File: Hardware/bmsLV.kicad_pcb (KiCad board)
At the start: 2 copper layers, 121.2 x 60.6 mm, 160 parts, among them J1 Conn_01x06_Male, J10 Conn_01x01_Female, J11 Conn_01x01_Female, J12 Conn_01x01_Female, J13 Conn_01x04_Male, J14 Conn_01x02_Male, J15 Conn_01x02_Male, J16 Conn_01x02_Male, J17 Conn_01x02_Male, J2 USB_B_Mini, J3 Conn_01x02_Female, J4 Conn_01x02_Male, J5 CAN conn, J6 Conn_01x01_Female, J7 Conn_01x01_Female, J8 Conn_01x01_Female, J9 Conn_01x01_Female, K1 RM85V7, Q1 BSS138, Q2 Q_NMOS_GSD, Q3 Q_NMOS_GSD, Q4 Q_NMOS_GSD, Q5 Q_NMOS_GSD, Q6 Q_NMOS_GSD, Q7 Q_NMOS_GSD, Q8 BSS138, Q9 Q_NPN_BCE, SW1 SW_Push, U2 LM1117-3.3, U3 LM2596S-5, U4 MCP2562-H-SN, U5 STM32L4P5RET6, Y1 Crystal

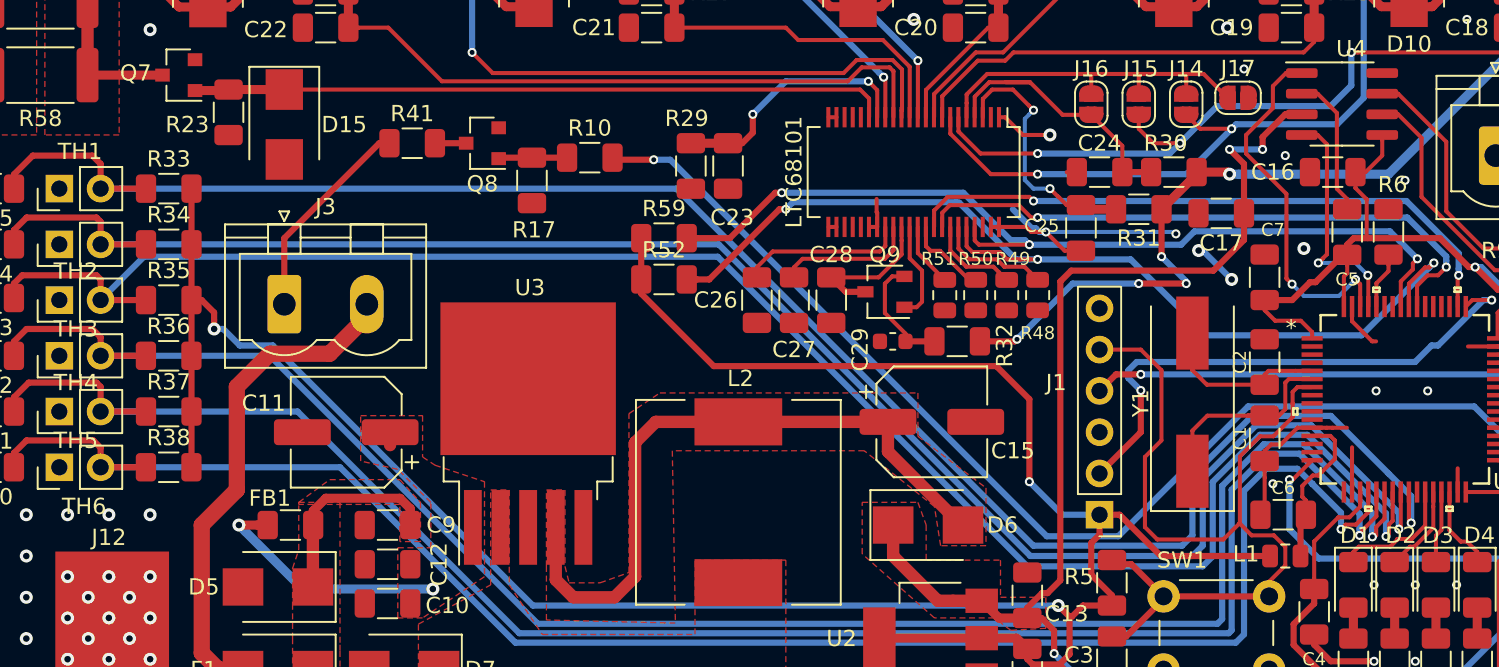
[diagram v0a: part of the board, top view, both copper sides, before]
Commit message: CS and CLK pull up added
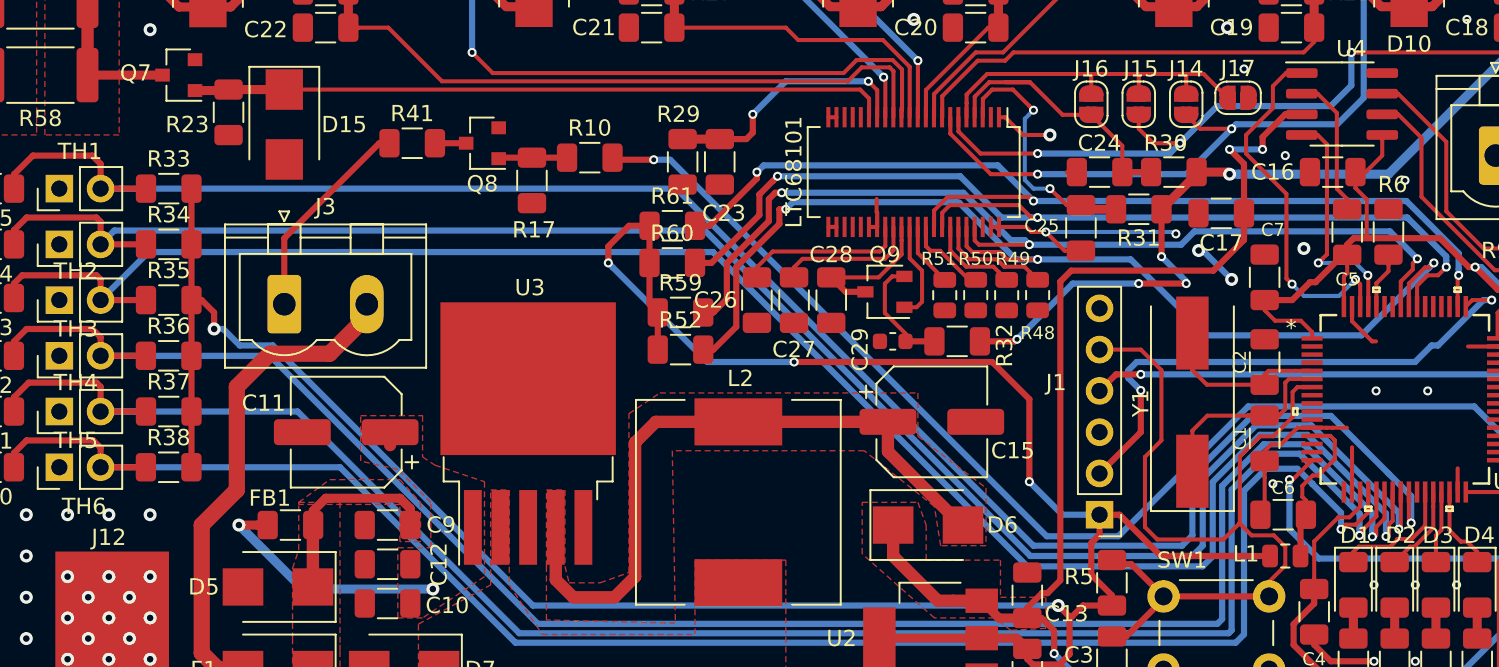
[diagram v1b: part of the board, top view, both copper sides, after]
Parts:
- added R60: 2.2k, Resistor_SMD:R_1206_3216Metric, F.Cu at (62.6, 89.9)
- added R61: 2.2k, Resistor_SMD:R_1206_3216Metric, F.Cu at (62.6, 87.6)
- moved R59 4.68 mm to (63.1, 93.0)
- moved R52 4.44 mm to (63.1, 95.2)
- moved C23 0.57 mm to (65.5, 83.7)
- moved R29 0.57 mm to (63.2, 83.7)
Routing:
- net SCK: track 37.6 -> 62.7 mm, vias 2 -> 3
- net CS: track 38.4 -> 61.9 mm, vias 2 -> 3
- net SW_VDD: track 274.8 -> 286.1 mm, vias 5 -> 7
- net MISO: track 62.6 -> 66.0 mm
- net MOSI: track 56.1 -> 59.1 mm
- net SW_GND: track 83.6 -> 81.0 mm
- net Term_5: track 110.7 -> 111.4 mm

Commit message: Checked By SS
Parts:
- moved R48 0.25 mm to (84.8, 91.9)
- moved R49 0.25 mm to (82.9, 91.9)
- moved R50 0.25 mm to (81.0, 91.9)
- moved R51 0.25 mm to (79.1, 91.9)
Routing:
- net SW_GND: track 81.0 -> 86.1 mm
- net Term_6: track 112.1 -> 109.4 mm
- net Term_4: track 111.3 -> 108.6 mm
- net Term_5: track 111.4 -> 109.0 mm
- net +24V: track 76.4 -> 74.3 mm, vias 118 -> 114
- net +5V: track 99.4 -> 97.6 mm
- net Term_1: track 106.6 -> 105.3 mm
- net Term_2: track 109.8 -> 108.6 mm
- net MISO: track 66.0 -> 64.8 mm
- net Term_3: track 111.5 -> 110.5 mm
- net TX_Can: track 22.6 -> 22.0 mm

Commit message: PUTM Logos added
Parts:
- added G***: LOGO, Logos:SignatureBox50mm, B.Cu at (66.0, 75.7)
- added G***: LOGO, Logos:PUTM_LOGO_35mm, B.Cu at (66.3, 101.9)
- added G***: LOGO, Logos:PUTM_LOGO_13mm, F.Cu at (54.4, 80.0)
- moved Q8 2.59 mm to (50.4, 85.1)
- moved R17 2.59 mm to (53.5, 87.4)
- moved R41 2.59 mm to (46.1, 85.1)
- moved R10 2.59 mm to (57.0, 86.0)
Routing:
- net Term_3: track 110.5 -> 106.4 mm
- net Term_2: track 108.6 -> 104.8 mm
- net LED_D: track 72.7 -> 74.1 mm
- net Term_1: track 105.3 -> 104.0 mm
- net LED_D_OUT: track 13.0 -> 12.0 mm
- net SW_GND: vias 59 -> 60

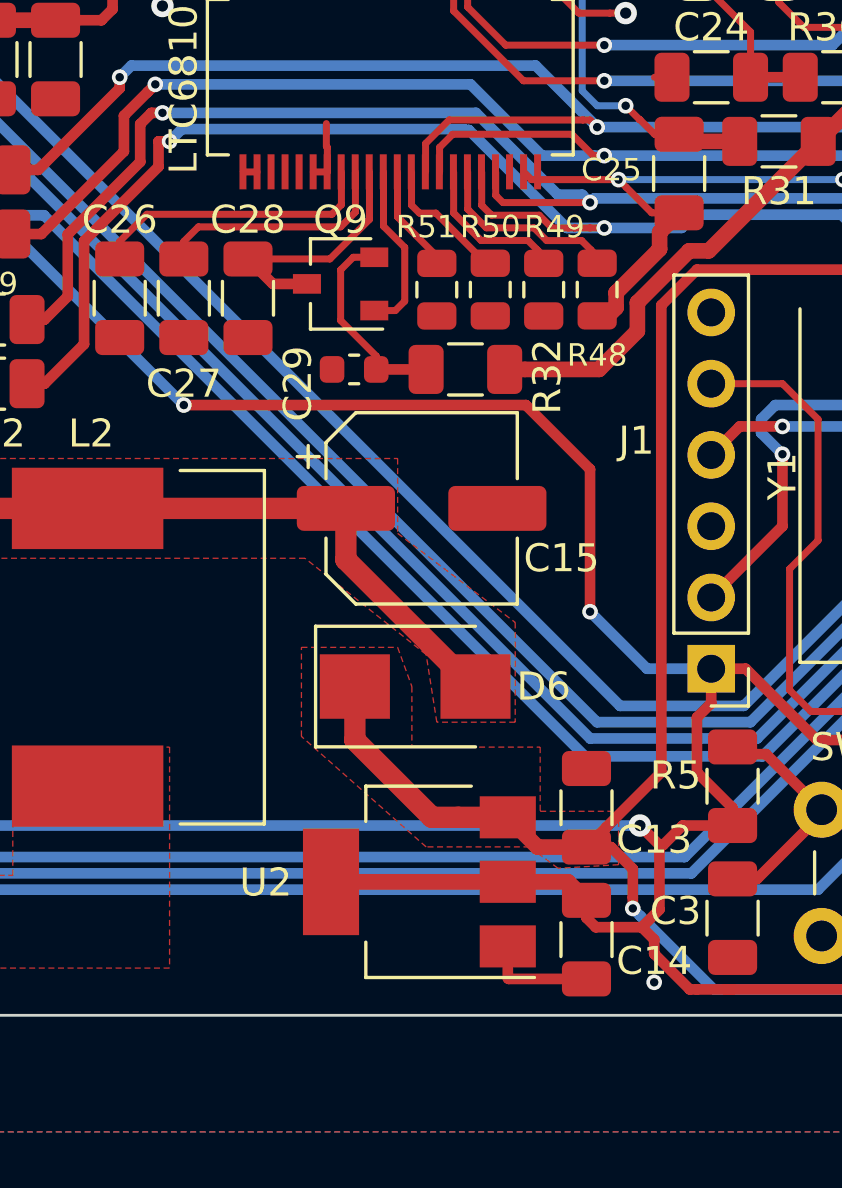
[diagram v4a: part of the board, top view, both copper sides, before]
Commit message: gitignore modified
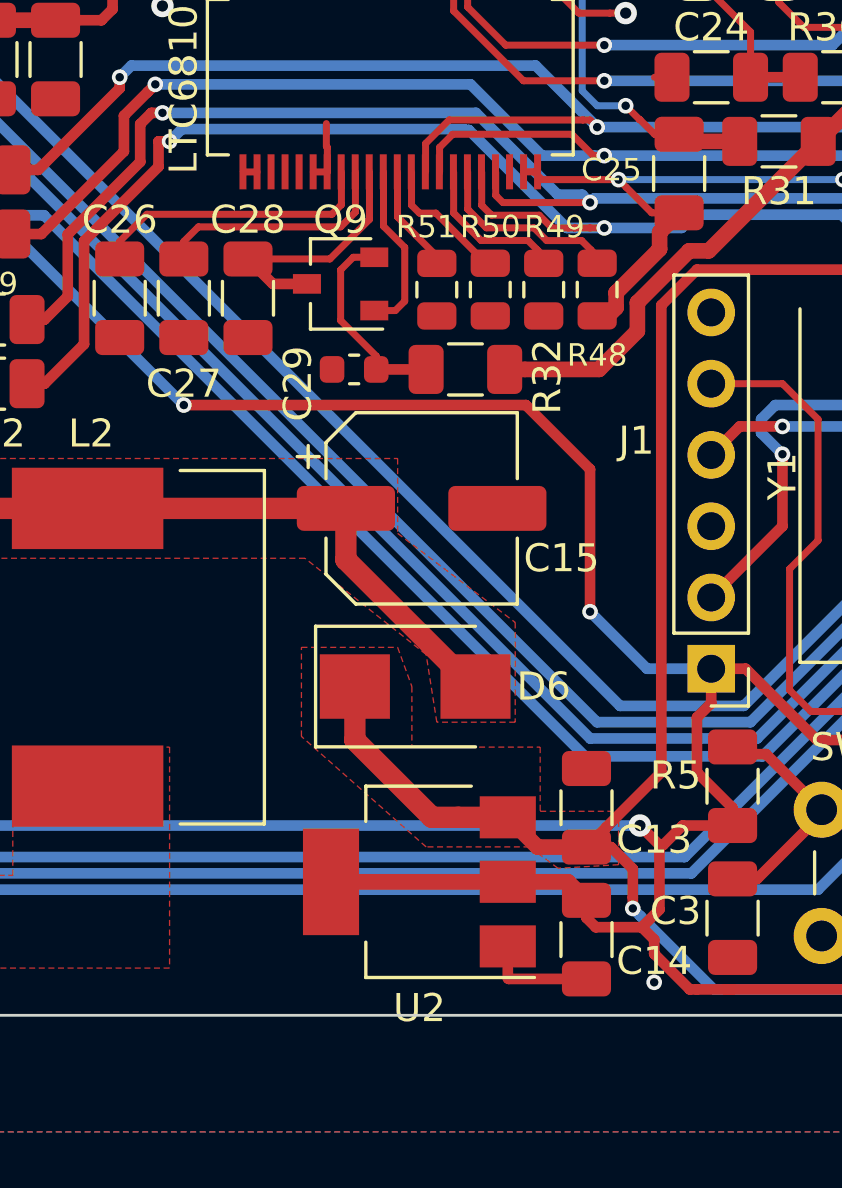
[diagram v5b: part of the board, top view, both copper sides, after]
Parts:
- U2: footprint Package_TO_SOT_SMD:SOT-223 -> Package_TO_SOT_SMD:SOT-223-3_TabPin2
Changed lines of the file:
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@@
     (thickness 1.6)
     (drawings 4)
-    (tracks 1311)
+    (tracks 1312)
     (zones 0)
     (modules 165)
@@
     (pcbplotparams
       (layerselection 0x010fc_ffffffff)
-      (usegerberextensions false)
+      (usegerberextensions true)
       (usegerberattributes false)
       (usegerberadvancedattributes false)
@@
       (psa4output false)
       (plotreference true)
-      (plotvalue true)
+      (plotvalue false)
       (plotinvisibletext false)
       (padsonsilk false)
-      (subtractmaskfromsilk false)
+      (subtractmaskfromsilk true)
       (outputformat 1)
       (mirror false)
-      (drillshape 1)
+      (drillshape 0)
       (scaleselection 1)
-      (outputdirectory ""))
+      (outputdirectory "PUTM_EV_BMS_LV_GERBERS/"))
   )
   (net 0 "")
@@
     (add_net V_Out)
   )
+  (module Package_TO_SOT_SMD:SOT-223-3_TabPin2 (layer F.Cu)
+    (at 78.5 113.005 180)
+    (descr "module CMS SOT223 4 pins")
+    (tags "CMS SOT")
+    (attr smd)
+    (fp_text reference U2 (at 0 -4.5) (layer F.SilkS)
+      (effects (font (size 1 1) (thickness 0.15)))
+    )
+    (fp_text value LM1117-3.3 (at 0 4.5) (layer F.Fab)
+      (effects (font (size 1 1) (thickness 0.15)))
+    )
+    (fp_line (start 1.85 -3.35) (end 1.85 3.35) (layer F.Fab) (width 0.1))
+    (fp_line (start -1.85 3.35) (end 1.85 3.35) (layer F.Fab) (width 0.1))
+    (fp_line (start -4.1 -3.41) (end 1.91 -3.41) (layer F.SilkS) (width 0.12))
+    (fp_line (start -0.85 -3.35) (end 1.85 -3.35) (layer F.Fab) (width 0.1))
+    (fp_line (start -1.85 3.41) (end 1.91 3.41) (layer F.SilkS) (width 0.12))
+    (fp_line (start -1.85 -2.35) (end -1.85 3.35) (layer F.Fab) (width 0.1))
+    (fp_line (start -1.85 -2.35) (end -0.85 -3.35) (layer F.Fab) (width 0.1))
+    (fp_line (start -4.4 -3.6) (end -4.4 3.6) (layer F.CrtYd) (width 0.05))
+    (fp_line (start -4.4 3.6) (end 4.4 3.6) (layer F.CrtYd) (width 0.05))
+    (fp_line (start 4.4 3.6) (end 4.4 -3.6) (layer F.CrtYd) (width 0.05))
+    (fp_line (start 4.4 -3.6) (end -4.4 -3.6) (layer F.CrtYd) (width 0.05))
+    (fp_line (start 1.91 -3.41) (end 1.91 -2.15) (layer F.SilkS) (width 0.12))
+    (fp_line (start 1.91 3.41) (end 1.91 2.15) (layer F.SilkS) (width 0.12))
+    (fp_text user %R (at 0 0 90) (layer F.Fab)
+      (effects (font (size 0.8 0.8) (thickness 0.12)))
+    )
+    (pad 1 smd rect (at -3.15 -2.3 180) (size 2 1.5) (layers F.Cu F.Paste F.Mask)
+      (net 1 SW_GND))
+    (pad 3 smd rect (at -3.15 2.3 180) (size 2 1.5) (layers F.Cu F.Paste F.Mask)
+      (net 6 +5V))
+    (pad 2 smd rect (at -3.15 0 180) (size 2 1.5) (layers F.Cu F.Paste F.Mask)
+      (net 3 SW_VDD))
+    (pad 2 smd rect (at 3.15 0 180) (size 2 3.8) (layers F.Cu F.Paste F.Mask)
+      (net 3 SW_VDD))
+    (model ${KISYS3DMOD}/Package_TO_SOT_SMD.3dshapes/SOT-223.wrl
+      (at (xyz 0 0 0))
+      (scale (xyz 1 1 1))
+      (rotate (xyz 0 0 0))
+    )
+  )
   (module Logos:SignatureBox50mm (layer B.Cu)
     (at 66.04 75.692)
@@
     )
   )
-  (module Package_TO_SOT_SMD:SOT-223 (layer F.Cu)
-    (at 78.5 113.005 180)
-    (descr "module CMS SOT223 4 pins")
-    (tags "CMS SOT")
-    (attr smd)
-    (fp_text reference U2 (at 5.475 -0.025 180) (layer F.SilkS)
-      (effects (font (size 1 1) (thickness 0.15)))
-    )
-    (fp_text value LM1117-3.3 (at 0 4.5) (layer F.Fab)
-      (effects (font (size 1 1) (thickness 0.15)))
-    )
-    (fp_text user %R (at 0 0 90) (layer F.Fab)
-      (effects (font (size 0.8 0.8) (thickness 0.12)))
-    )
-    (fp_line (start -1.85 -2.3) (end -0.8 -3.35) (layer F.Fab) (width 0.1))
-    (fp_line (start 1.91 3.41) (end 1.91 2.15) (layer F.SilkS) (width 0.12))
-    (fp_line (start 1.91 -3.41) (end 1.91 -2.15) (layer F.SilkS) (width 0.12))
-    (fp_line (start 4.4 -3.6) (end -4.4 -3.6) (layer F.CrtYd) (width 0.05))
-    (fp_line (start 4.4 3.6) (end 4.4 -3.6) (layer F.CrtYd) (width 0.05))
-    (fp_line (start -4.4 3.6) (end 4.4 3.6) (layer F.CrtYd) (width 0.05))
-    (fp_line (start -4.4 -3.6) (end -4.4 3.6) (layer F.CrtYd) (width 0.05))
-    (fp_line (start -1.85 -2.3) (end -1.85 3.35) (layer F.Fab) (width 0.1))
-    (fp_line (start -1.85 3.41) (end 1.91 3.41) (layer F.SilkS) (width 0.12))
-    (fp_line (start -0.8 -3.35) (end 1.85 -3.35) (layer F.Fab) (width 0.1))
-    (fp_line (start -4.1 -3.41) (end 1.91 -3.41) (layer F.SilkS) (width 0.12))
-    (fp_line (start -1.85 3.35) (end 1.85 3.35) (layer F.Fab) (width 0.1))
-    (fp_line (start 1.85 -3.35) (end 1.85 3.35) (layer F.Fab) (width 0.1))
-    (pad 4 smd rect (at 3.15 0 180) (size 2 3.8) (layers F.Cu F.Paste F.Mask))
-    (pad 2 smd rect (at -3.15 0 180) (size 2 1.5) (layers F.Cu F.Paste F.Mask)
-      (net 3 SW_VDD))
-    (pad 3 smd rect (at -3.15 2.3 180) (size 2 1.5) (layers F.Cu F.Paste F.Mask)
-      (net 6 +5V))
-    (pad 1 smd rect (at -3.15 -2.3 180) (size 2 1.5) (layers F.Cu F.Paste F.Mask)
-      (net 1 SW_GND))
-    (model ${KISYS3DMOD}/Package_TO_SOT_SMD.3dshapes/SOT-223.wrl
-      (at (xyz 0 0 0))
-      (scale (xyz 1 1 1))
-      (rotate (xyz 0 0 0))
-    )
-  )
   (module Button_Switch_THT:SW_PUSH_6mm (layer F.Cu)
     (at 92.837 110.435)
@@
   (segment (start 85.876999 88.255489) (end 85.598 87.97649) (width 0.25) (layer F.Cu) (net 1))
   (segment (start 87.757 89.16) (end 86.78151 89.16) (width 0.25) (layer F.Cu) (net 1))
-  (segment (start 85.203435 87.97649) (end 85.598 87.97649) (width 0.25) (layer F.Cu) (net 1))
-  (segment (start 82.49349 87.97649) (end 85.203435 87.97649) (width 0.25) (layer F.Cu) (net 1))
-  (segment (start 82.22 87.703) (end 82.49349 87.97649) (width 0.25) (layer F.Cu) (net 1))
   (via (at 93.599 87.97649) (size 0.558) (drill 0.3) (layers F.Cu B.Cu) (net 1))
   (segment (start 87.06129 89.85571) (end 87.757 89.16) (width 0.5588) (layer F.Cu) (net 1))
@@
   (segment (start 84.836 92.8324) (end 85.2216 92.8324) (width 0.5588) (layer F.Cu) (net 1))
   (via (at 69.342 81.788) (size 0.8) (drill 0.4) (layers F.Cu B.Cu) (net 1))
+  (segment (start 82.86389 87.97649) (end 85.203435 87.97649) (width 0.25) (layer F.Cu) (net 1))
+  (segment (start 85.203435 87.97649) (end 85.598 87.97649) (width 0.25) (layer F.Cu) (net 1))
+  (segment (start 82.5872 87.6998) (end 82.86389 87.97649) (width 0.25) (layer F.Cu) (net 1))
+  (segment (start 82.2122 87.6998) (end 82.5872 87.6998) (width 0.25) (layer F.Cu) (net 1))
   (segment (start 91.44 95.25) (end 88.9 95.25) (width 0.25) (layer F.Cu) (net 2))
   (segment (start 92.71 100.838) (end 92.71 96.52) (width 0.25) (layer F.Cu) (net 2))
